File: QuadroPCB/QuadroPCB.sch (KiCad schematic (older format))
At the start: 3 parts

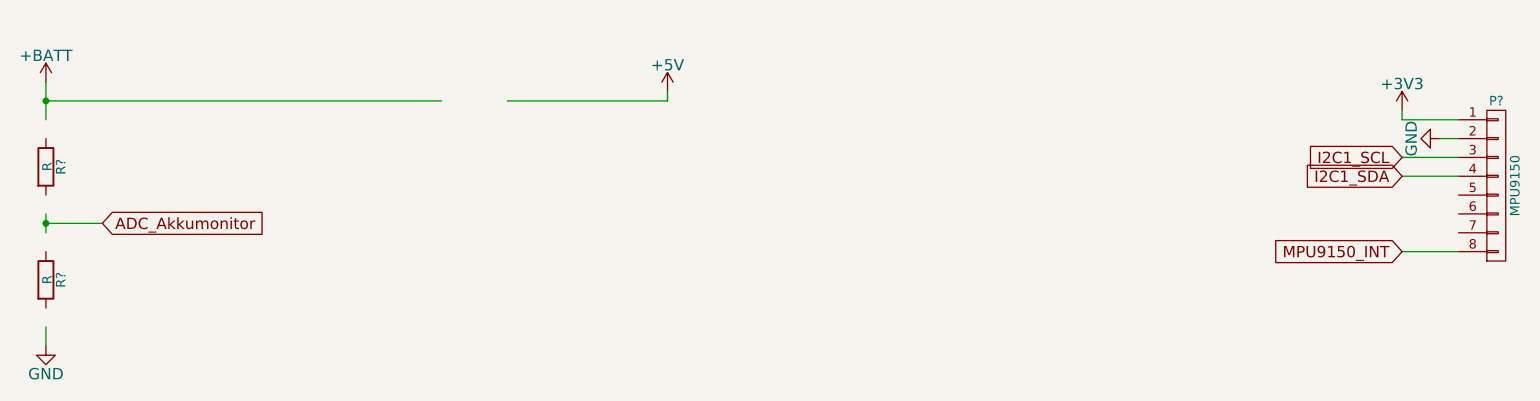
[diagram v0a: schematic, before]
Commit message: added datasheets add step-down converter
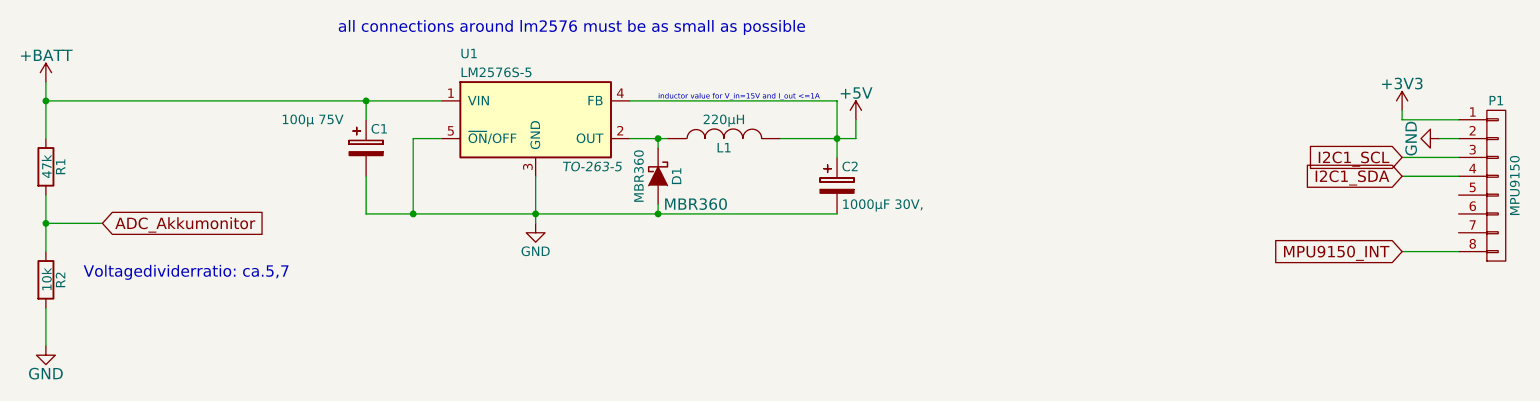
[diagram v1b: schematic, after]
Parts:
- added C1: 100µ 75V, symbol CP
- added C2: 1000µF 30V,, symbol CP
- added D1: MBR360, symbol D_Schottky
- added L1: 220µH, symbol INDUCTOR
- added U1: LM2576S-5, TO-263-5, symbol LM2576S-5
- R1: renamed from R?; value R -> 47k
- R2: renamed from R?; value R -> 10k
- gave numbers to parts that had none: 1
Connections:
- wire segments 13 -> 24
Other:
- note added: "Voltagedividerratio: ca.5,7\n"
- note added: "all connections around lm2576 must be as small as possible"
- note added: "inductor value for V_in=15V and I_out <=1A"
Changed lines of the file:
@@
 LIBS:contrib
 LIBS:valves
+LIBS:dc-dc
+LIBS:stm32
+LIBS:sensors
+LIBS:QuadroPCB-cache
 EELAYER 25 0
 EELAYER END
@@
 $EndDescr
 $Comp
-L R R?
+L R R1
 U 1 1 553FEDF5
 P 1350 1350
-F 0 "R?" V 1430 1350 50  0000 C CNN
-F 1 "R" V 1357 1351 50  0000 C CNN
+F 0 "R1" V 1430 1350 50  0000 C CNN
+F 1 "47k" V 1357 1351 50  0000 C CNN
 F 2 "" V 1280 1350 30  0000 C CNN
 F 3 "" H 1350 1350 30  0000 C CNN
@@
 $EndComp
 $Comp
-L R R?
+L R R2
 U 1 1 553FEF71
 P 1350 1950
-F 0 "R?" V 1430 1950 50  0000 C CNN
-F 1 "R" V 1357 1951 50  0000 C CNN
+F 0 "R2" V 1430 1950 50  0000 C CNN
+F 1 "10k" V 1357 1951 50  0000 C CNN
 F 2 "" V 1280 1950 30  0000 C CNN
 F 3 "" H 1350 1950 30  0000 C CNN
@@
 $EndComp
 $Comp
-L GND #PWR?
+L GND #PWR2
 U 1 1 553FEFAB
 P 1350 2300
-F 0 "#PWR?" H 1350 2050 60  0001 C CNN
+F 0 "#PWR2" H 1350 2050 60  0001 C CNN
 F 1 "GND" H 1350 2150 60  0000 C CNN
 F 2 "" H 1350 2300 60  0000 C CNN
@@
 $EndComp
 $Comp
-L +BATT #PWR?
+L +BATT #PWR1
 U 1 1 553FEFC1
 P 1350 900
-F 0 "#PWR?" H 1350 750 60  0001 C CNN
+F 0 "#PWR1" H 1350 750 60  0001 C CNN
 F 1 "+BATT" H 1350 1040 60  0000 C CNN
 F 2 "" H 1350 900 60  0000 C CNN
@@
 $EndComp
 Wire Wire Line
-	1350 2300 1350 2200
-Wire Wire Line
-	1350 1600 1350 1700
-Wire Wire Line
-	1350 900  1350 1100
+	1350 2100 1350 2300
+Wire Wire Line
+	1350 1500 1350 1800
+Wire Wire Line
+	1350 900  1350 1200
 Text GLabel 1650 1650 2    60   Input ~ 0
 ADC_Akkumonitor
@@
 	1350 1000 3450 1000
 Connection ~ 1350 1000
-Wire Wire Line
-	3800 1000 4650 1000
-$Comp
-L +5V #PWR?
+$Comp
+L +5V #PWR4
 U 1 1 553FF02F
-P 4650 950
-F 0 "#PWR?" H 4650 800 60  0001 C CNN
-F 1 "+5V" H 4650 1090 60  0000 C CNN
-F 2 "" H 4650 950 60  0000 C CNN
-F 3 "" H 4650 950 60  0000 C CNN
-	1    4650 950
-	1    0    0    -1
-$EndComp
-Wire Wire Line
-	4650 1000 4650 950
-$Comp
-L CONN_01X08 P?
+P 5650 1100
+F 0 "#PWR4" H 5650 950 60  0001 C CNN
+F 1 "+5V" H 5650 1240 60  0000 C CNN
+F 2 "" H 5650 1100 60  0000 C CNN
+F 3 "" H 5650 1100 60  0000 C CNN
+	1    5650 1100
+	1    0    0    -1
+$EndComp
+Wire Wire Line
+	5650 1200 5650 1100
+$Comp
+L CONN_01X08 P1
 U 1 1 553FF0BA
 P 9050 1450
-F 0 "P?" H 9050 1900 50  0000 C CNN
+F 0 "P1" H 9050 1900 50  0000 C CNN
 F 1 "MPU9150" V 9150 1450 50  0000 C CNN
 F 2 "" H 9050 1450 60  0000 C CNN
@@
 $EndComp
 $Comp
-L GND #PWR?
+L GND #PWR6
 U 1 1 553FF2AD
 P 8750 1200
-F 0 "#PWR?" H 8750 950 60  0001 C CNN
+F 0 "#PWR6" H 8750 950 60  0001 C CNN
 F 1 "GND" H 8750 1050 60  0000 C CNN
 F 2 "" H 8750 1200 60  0000 C CNN
@@
 $EndComp
 $Comp
-L +3V3 #PWR?
+L +3V3 #PWR5
 U 1 1 553FF331
 P 8550 1050
-F 0 "#PWR?" H 8550 900 60  0001 C CNN
+F 0 "#PWR5" H 8550 900 60  0001 C CNN
 F 1 "+3V3" H 8550 1190 60  0000 C CNN
 F 2 "" H 8550 1050 60  0000 C CNN
@@
 Wire Wire Line
 	8850 1800 8550 1800
+Text Notes 1550 1950 0    60   ~ 0
+Voltagedividerratio: ca.5,7\n
+$Comp
+L LM2576S-5 U1
+U 1 1 5541EC13
+P 3950 1100
+F 0 "U1" H 3550 1450 50  0000 L CNN
+F 1 "LM2576S-5" H 3550 1350 50  0000 L CNN
+F 2 "TO-263-5" H 4250 850 50  0000 C CIN
+F 3 "" H 3950 1100 50  0000 C CNN
+	1    3950 1100
+	1    0    0    -1
+$EndComp
+$Comp
+L GND #PWR3
+U 1 1 5541ECA6
+P 3950 1650
+F 0 "#PWR3" H 3950 1400 50  0001 C CNN
+F 1 "GND" H 3950 1500 50  0000 C CNN
+F 2 "" H 3950 1650 60  0000 C CNN
+F 3 "" H 3950 1650 60  0000 C CNN
+	1    3950 1650
+	1    0    0    -1
+$EndComp
+Wire Wire Line
+	3950 1400 3950 1650
+Wire Wire Line
+	3450 1200 3300 1200
+Wire Wire Line
+	3300 1200 3300 1600
+Wire Wire Line
+	3050 1600 5550 1600
+Connection ~ 3950 1600
+$Comp
+L INDUCTOR L1
+U 1 1 5541EE99
+P 4950 1200
+F 0 "L1" V 4900 1200 50  0000 C CNN
+F 1 "220µH" V 5050 1200 50  0000 C CNN
+F 2 "" H 4950 1200 60  0000 C CNN
+F 3 "" H 4950 1200 60  0000 C CNN
+	1    4950 1200
+	0    -1   -1   0
+$EndComp
+$Comp
+L CP C2
+U 1 1 5541EF3E
+P 5550 1450
+F 0 "C2" H 5575 1550 50  0000 L CNN
+F 1 "1000µF 30V," H 5575 1350 50  0000 L CNN
+F 2 "" H 5588 1300 30  0000 C CNN
+F 3 "" H 5550 1450 60  0000 C CNN
+	1    5550 1450
+	1    0    0    -1
+$EndComp
+$Comp
+L CP C1
+U 1 1 5541EF75
+P 3050 1250
+F 0 "C1" H 3075 1350 50  0000 L CNN
+F 1 "100µ 75V" H 2600 1400 50  0000 L CNN
+F 2 "" H 3088 1100 30  0000 C CNN
+F 3 "" H 3050 1250 60  0000 C CNN
+	1    3050 1250
+	1    0    0    -1
+$EndComp
+Wire Wire Line
+	3050 1400 3050 1600
+Connection ~ 3300 1600
+Wire Wire Line
+	3050 1100 3050 1000
+Connection ~ 3050 1000
+Wire Wire Line
+	4450 1200 4650 1200
+Wire Wire Line
+	5250 1200 5650 1200
+Connection ~ 5550 1200
+$Comp
+L D_Schottky D1
+U 1 1 5541F140
+P 4600 1400
+F 0 "D1" H 4600 1500 50  0000 C CNN
+F 1 "MBR360" H 4600 1300 50  0000 C CNN
+F 2 "" H 4600 1400 60  0000 C CNN
+F 3 "" H 4600 1400 60  0000 C CNN
+F 4 "MBR360" V 4750 1600 60  0000 C CNN "type"
+	1    4600 1400
+	0    1    1    0
+$EndComp
+Wire Wire Line
+	4600 1250 4600 1200
+Connection ~ 4600 1200
+Wire Wire Line
+	4600 1550 4600 1600
+Connection ~ 4600 1600
+Wire Wire Line
+	5550 1000 5550 1300
+Text Notes 2900 650  0    60   ~ 0
+all connections around lm2576 must be as small as possible
+Text Notes 4600 1000 0    28   ~ 0
+inductor value for V_in=15V and I_out <=1A
+Wire Wire Line
+	5550 1000 4450 1000
 $EndSCHEMATC

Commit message: Updated schematic rc receiver, bmp180, motor, eeprom added more datasheets
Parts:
- added IC?: AT24CS02-SSHM, SO8, symbol AT24CS02-SSHM
- added P?: CONN_01X04, symbol CONN_01X04
- added P? (x2): CONN_02X25, symbol CONN_02X25
- added P? (x5): CONN_01X03, symbol CONN_01X03
- added Q?: BSS123, symbol Q_NMOS_DGS
- added R?: 1k, symbol R
- added R? (x2): 10k, symbol R
- added SP?: SPEAKER, symbol SPEAKER
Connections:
- net labels added: +3.3V, Beeper_PIN, I2C2_SCL, I2C2_SDA, MOTOR1, MOTOR2, MOTOR3, MOTOR4, RC_Signal
- wire segments 24 -> 100
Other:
- note added: "BMP180"
- note added: "Beeper"
- note added: "EEPROM\n"
- note added: "MPU9150"
- note added: "Motor Connectors\n"
- note added: "Power\n"
- note added: "RC Receiver"
- note added: "STM32F3 Discovery\n\nPin Headers\n"
- note added: "left\n"
- note added: "right\n"
- moved on the sheet: C1, C2, D1, L1, P1, R1, R2, U1

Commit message: updated connections
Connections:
- net labels added: PA1, PA10, PA9, PB6, PB7, PB8, PC6, PC7, PC8, PC9, PE4
- wire segments 100 -> 123
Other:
- note added: "Connections\n"
- note added: "TODO:\n\nbuzzer pin\nweite pins rausführen?\n"
- moved on the sheet: P?

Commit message: blub
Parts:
- removed Q?: BSS123, symbol Q_NMOS_DGS
- added P10: AKKU, Wire_Connections_Bridges:WireConnection_1-2mmDrill, symbol CONN_01X02
- added Q1: Q_NMOS_GSD, Housings_SOT-23_SOT-143_TSOT-6:SOT-23_Handsoldering, symbol Q_NMOS_GSD
- C1: value 100µ 75V -> 100µ 25V; footprint (none) -> Capacitors_SMD:c_elec_6.3x7.7
- C2: value 1000µF 30V, -> 680µF 10V; footprint (none) -> Capacitors_SMD:c_elec_8x10
- D1: footprint (none) -> Diodes_SMD:Diode-DO-214BA
- IC1: renamed from IC?; footprint SO8 -> Sockets_DIP:DIP-8__300_ELL
- L1: footprint (none) -> Choke_SMD:Choke_SMD_PISR_Handsoldering_FASTRON
- P1: footprint (none) -> Pin_Headers:Pin_Header_Straight_1x08
- P2: renamed from P?; value CONN_02X25 -> stm32discovery_left; footprint (none) -> Pin_Headers:Pin_Header_Straight_2x25
- P3: renamed from P?; value CONN_02X25 -> stm32discovery_right; footprint (none) -> Pin_Headers:Pin_Header_Straight_2x25
- P4: renamed from P?; value CONN_01X03 -> rc_signal; footprint (none) -> Pin_Headers:Pin_Header_Straight_1x03
- P5: renamed from P?; value CONN_01X03 -> Motor3; footprint (none) -> Pin_Headers:Pin_Header_Straight_1x03
- P6: renamed from P?; value CONN_01X03 -> Motor4; footprint (none) -> Pin_Headers:Pin_Header_Straight_1x03
- P7: renamed from P?; value CONN_01X04 -> BMP180; footprint (none) -> Pin_Headers:Pin_Header_Straight_1x04
- P8: renamed from P?; value CONN_01X03 -> Motor1; footprint (none) -> Pin_Headers:Pin_Header_Straight_1x03
- P9: renamed from P?; value CONN_01X03 -> Motor2; footprint (none) -> Pin_Headers:Pin_Header_Straight_1x03
- R1, R2: footprint (none) -> Resistors_SMD:R_0805_HandSoldering
- R3, R4, R5: renamed from R?; footprint (none) -> Resistors_SMD:R_0805_HandSoldering
- SP1: renamed from SP?; footprint (none) -> Buzzers_Beepers:Buzzer_12x9.5RM7.6
- U1: footprint TO-263-5 -> SMD_Packages:TO-263-5_HandSoldering
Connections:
- net labels added: power_gnd, pwr
- wire segments 123 -> 109
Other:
- moved on the sheet: R1, R2

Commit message: dei mudder commitet
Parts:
- P10: footprint Wire_Connections_Bridges:WireConnection_1-2mmDrill -> Connect:PINHEAD1-2
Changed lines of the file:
@@
 F 0 "P10" H 1000 1750 50  0000 C CNN
 F 1 "AKKU" V 1100 1600 50  0000 C CNN
-F 2 "Wire_Connections_Bridges:WireConnection_1-2mmDrill" H 1000 1600 60  0001 C CNN
+F 2 "Connect:PINHEAD1-2" H 1000 1600 60  0001 C CNN
 F 3 "" H 1000 1600 60  0000 C CNN
 	1    1000 1600

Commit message: neuer step down
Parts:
- removed U1: LM2576S-5, SMD_Packages:TO-263-5_HandSoldering, symbol LM2576S-5
- added C3: 10nF, Capacitors_SMD:C_0805_HandSoldering, symbol C
- added U1: LM2675M-5, SMD_Packages:SOIC-8-N, symbol LM2675M-5
- C1: value 100µ 25V -> 220µF 25V; footprint Capacitors_SMD:c_elec_6.3x7.7 -> Capacitors_SMD:c_elec_8x10.5
- C2: value 680µF 10V -> 100µF 10V; footprint Capacitors_SMD:c_elec_8x10 -> Capacitors_SMD:c_elec_8x6.7
- D1: value MBR360 -> MBRS340; footprint Diodes_SMD:Diode-DO-214BA -> Diodes_SMD:Diode-DO-214AB_Handsoldering; type MBR360 -> (none)
- L1: value 220µH -> 33µH 1,4 A; footprint Choke_SMD:Choke_SMD_PISR_Handsoldering_FASTRON -> Choke_SMD:Choke_SMD_PISN_Handsoldering_FASTRON
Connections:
- net +5V: now also U1.4 (FB)
- net +BATT: now also U1.7 (VIN)
- net GND: now also U1.6 (GND)
- net pwr: no longer names the net of D1.1 (K), L1.1
- net pwr: now also C3.1, U1.8 (VSW)
- new net: C3.2, U1.1 (CB)
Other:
- note removed: "all connections around lm2576 must be as small as possible"
- note removed: "inductor value for V_in=15V and I_out <=1A"
- moved on the sheet: D1, L1
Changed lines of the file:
@@
 $EndComp
 $Comp
-L GND #PWR01
+L GND #PWR5
 U 1 1 553FEFAB
 P 1550 2150
-F 0 "#PWR01" H 1550 1900 60  0001 C CNN
+F 0 "#PWR5" H 1550 1900 60  0001 C CNN
 F 1 "GND" H 1550 2000 60  0000 C CNN
 F 2 "" H 1550 2150 60  0000 C CNN
@@
 $EndComp
 $Comp
-L +BATT #PWR02
+L +BATT #PWR4
 U 1 1 553FEFC1
 P 1550 1000
-F 0 "#PWR02" H 1550 850 60  0001 C CNN
+F 0 "#PWR4" H 1550 850 60  0001 C CNN
 F 1 "+BATT" H 1550 1140 60  0000 C CNN
 F 2 "" H 1550 1000 60  0000 C CNN
@@
 	1900 1600 1550 1600
 Connection ~ 1550 1600
-Wire Wire Line
-	1350 1100 3200 1100
 Connection ~ 1550 1100
 $Comp
-L +5V #PWR03
+L +5V #PWR11
 U 1 1 553FF02F
 P 5400 1200
-F 0 "#PWR03" H 5400 1050 60  0001 C CNN
+F 0 "#PWR11" H 5400 1050 60  0001 C CNN
 F 1 "+5V" H 5400 1340 60  0000 C CNN
 F 2 "" H 5400 1200 60  0000 C CNN
@@
 $EndComp
 $Comp
-L GND #PWR04
+L GND #PWR15
 U 1 1 553FF2AD
 P 8700 1150
-F 0 "#PWR04" H 8700 900 60  0001 C CNN
+F 0 "#PWR15" H 8700 900 60  0001 C CNN
 F 1 "GND" H 8700 1000 60  0000 C CNN
 F 2 "" H 8700 1150 60  0000 C CNN
@@
 $EndComp
 $Comp
-L +3V3 #PWR05
+L +3V3 #PWR14
 U 1 1 553FF331
 P 8500 1000
-F 0 "#PWR05" H 8500 850 60  0001 C CNN
+F 0 "#PWR14" H 8500 850 60  0001 C CNN
 F 1 "+3V3" H 8500 1140 60  0000 C CNN
 F 2 "" H 8500 1000 60  0000 C CNN
@@
 Voltagedividerratio: ca.5,7\n
 $Comp
-L LM2576S-5 U1
-U 1 1 5541EC13
-P 3700 1200
-F 0 "U1" H 3300 1550 50  0000 L CNN
-F 1 "LM2576S-5" H 3300 1450 50  0000 L CNN
-F 2 "SMD_Packages:TO-263-5_HandSoldering" H 4000 950 50  0000 C CIN
-F 3 "" H 3700 1200 50  0000 C CNN
-	1    3700 1200
-	1    0    0    -1
-$EndComp
-$Comp
-L GND #PWR06
+L GND #PWR10
 U 1 1 5541ECA6
 P 3700 1750
-F 0 "#PWR06" H 3700 1500 50  0001 C CNN
+F 0 "#PWR10" H 3700 1500 50  0001 C CNN
 F 1 "GND" H 3700 1600 50  0000 C CNN
 F 2 "" H 3700 1750 60  0000 C CNN
@@
 $EndComp
 Wire Wire Line
-	3700 1500 3700 1750
-Wire Wire Line
-	3200 1300 3050 1300
-Wire Wire Line
-	3050 1300 3050 1700
-Wire Wire Line
 	2800 1700 5300 1700
 Connection ~ 3700 1700
@@
 L INDUCTOR L1
 U 1 1 5541EE99
-P 4700 1300
-F 0 "L1" V 4650 1300 50  0000 C CNN
-F 1 "220µH" V 4800 1300 50  0000 C CNN
-F 2 "Choke_SMD:Choke_SMD_PISR_Handsoldering_FASTRON" H 4700 1300 60  0001 C CNN
-F 3 "" H 4700 1300 60  0000 C CNN
-	1    4700 1300
+P 4900 1300
+F 0 "L1" V 4850 1300 50  0000 C CNN
+F 1 "33µH 1,4 A" V 5000 1300 50  0000 C CNN
+F 2 "Choke_SMD:Choke_SMD_PISN_Handsoldering_FASTRON" H 4900 1300 60  0001 C CNN
+F 3 "" H 4900 1300 60  0000 C CNN
+	1    4900 1300
 	0    -1   -1   0
 $EndComp
@@
 P 5300 1550
 F 0 "C2" H 5325 1650 50  0000 L CNN
-F 1 "680µF 10V" H 5325 1450 50  0000 L CNN
-F 2 "Capacitors_SMD:c_elec_8x10" H 5338 1400 30  0001 C CNN
+F 1 "100µF 10V" H 5325 1450 50  0000 L CNN
+F 2 "Capacitors_SMD:c_elec_8x6.7" H 5338 1400 30  0001 C CNN
 F 3 "" H 5300 1550 60  0000 C CNN
 	1    5300 1550
@@
 P 2800 1350
 F 0 "C1" H 2825 1450 50  0000 L CNN
-F 1 "100µ 25V" H 2350 1500 50  0000 L CNN
-F 2 "Capacitors_SMD:c_elec_6.3x7.7" H 2838 1200 30  0001 C CNN
+F 1 "220µF 25V" H 2350 1500 50  0000 L CNN
+F 2 "Capacitors_SMD:c_elec_8x10.5" H 2838 1200 30  0001 C CNN
 F 3 "" H 2800 1350 60  0000 C CNN
 	1    2800 1350
@@
 Wire Wire Line
 	2800 1500 2800 1700
-Connection ~ 3050 1700
-Wire Wire Line
-	2800 1200 2800 1100
+Wire Wire Line
+	2800 900  2800 1200
 Connection ~ 2800 1100
 Wire Wire Line
-	4200 1300 4400 1300
-Wire Wire Line
-	5000 1300 5400 1300
+	4200 1300 4600 1300
+Wire Wire Line
+	5200 1300 5400 1300
 Connection ~ 5300 1300
 $Comp
 L D_Schottky D1
 U 1 1 5541F140
-P 4350 1500
-F 0 "D1" H 4350 1600 50  0000 C CNN
-F 1 "MBR360" H 4350 1400 50  0000 C CNN
-F 2 "Diodes_SMD:Diode-DO-214BA" H 4350 1500 60  0001 C CNN
-F 3 "" H 4350 1500 60  0000 C CNN
-F 4 "MBR360" V 4500 1700 60  0000 C CNN "type"
-	1    4350 1500
+P 4550 1500
+F 0 "D1" H 4550 1600 50  0000 C CNN
+F 1 "MBRS340" H 4550 1400 50  0000 C CNN
+F 2 "Diodes_SMD:Diode-DO-214AB_Handsoldering" H 4550 1500 60  0001 C CNN
+F 3 "" H 4550 1500 60  0000 C CNN
+	1    4550 1500
 	0    1    1    0
 $EndComp
 Wire Wire Line
-	4350 1350 4350 1300
-Connection ~ 4350 1300
-Wire Wire Line
-	4350 1650 4350 1700
-Connection ~ 4350 1700
-Wire Wire Line
-	5300 1100 5300 1400
-Text Notes 2650 750  0    60   ~ 0
-all connections around lm2576 must be as small as possible
-Text Notes 4350 1100 0    28   ~ 0
-inductor value for V_in=15V and I_out <=1A
-Wire Wire Line
-	5300 1100 4200 1100
+	4550 1100 4550 1350
+Connection ~ 4550 1300
+Wire Wire Line
+	4550 1650 4550 1700
+Connection ~ 4550 1700
 $Comp
 L R R4
@@
 $EndComp
 $Comp
-L +5V #PWR07
+L +5V #PWR22
 U 1 1 554200B8
 P 10600 900
-F 0 "#PWR07" H 10600 750 50  0001 C CNN
+F 0 "#PWR22" H 10600 750 50  0001 C CNN
 F 1 "+5V" H 10600 1040 50  0000 C CNN
 F 2 "" H 10600 900 60  0000 C CNN
@@
 $EndComp
 $Comp
-L GND #PWR08
+L GND #PWR23
 U 1 1 55420164
 P 10600 1750
-F 0 "#PWR08" H 10600 1500 50  0001 C CNN
+F 0 "#PWR23" H 10600 1500 50  0001 C CNN
 F 1 "GND" H 10600 1600 50  0000 C CNN
 F 2 "" H 10600 1750 60  0000 C CNN
@@
 $EndComp
 $Comp
-L GND #PWR09
+L GND #PWR21
 U 1 1 55420E59
 P 10400 2600
-F 0 "#PWR09" H 10400 2350 60  0001 C CNN
+F 0 "#PWR21" H 10400 2350 60  0001 C CNN
 F 1 "GND" H 10400 2450 60  0000 C CNN
 F 2 "" H 10400 2600 60  0000 C CNN
@@
 $EndComp
 $Comp
-L +3V3 #PWR010
+L +3V3 #PWR18
 U 1 1 5542137E
 P 10000 3350
-F 0 "#PWR010" H 10000 3200 60  0001 C CNN
+F 0 "#PWR18" H 10000 3200 60  0001 C CNN
 F 1 "+3V3" H 10000 3490 60  0000 C CNN
 F 2 "" H 10000 3350 60  0000 C CNN
@@
 $EndComp
 $Comp
-L GND #PWR011
+L GND #PWR19
 U 1 1 554213A3
 P 10000 4200
-F 0 "#PWR011" H 10000 3950 60  0001 C CNN
+F 0 "#PWR19" H 10000 3950 60  0001 C CNN
 F 1 "GND" H 10000 4050 60  0000 C CNN
 F 2 "" H 10000 4200 60  0000 C CNN
@@
 $EndComp
 $Comp
-L +3V3 #PWR012
+L +3V3 #PWR20
 U 1 1 55420E36
 P 10300 2300
-F 0 "#PWR012" H 10300 2150 60  0001 C CNN
+F 0 "#PWR20" H 10300 2150 60  0001 C CNN
 F 1 "+3V3" H 10300 2440 60  0000 C CNN
 F 2 "" H 10300 2300 60  0000 C CNN
@@
 	3600 2550 700  2550
 $Comp
-L +3V3 #PWR013
+L +3V3 #PWR1
 U 1 1 55422E4A
 P 1100 3300
-F 0 "#PWR013" H 1100 3150 60  0001 C CNN
+F 0 "#PWR1" H 1100 3150 60  0001 C CNN
 F 1 "+3V3" H 1100 3440 60  0000 C CNN
 F 2 "" H 1100 3300 60  0000 C CNN
@@
 $EndComp
 $Comp
-L +3V3 #PWR014
+L +3V3 #PWR6
 U 1 1 55422ECC
 P 1850 3300
-F 0 "#PWR014" H 1850 3150 60  0001 C CNN
+F 0 "#PWR6" H 1850 3150 60  0001 C CNN
 F 1 "+3V3" H 1850 3440 60  0000 C CNN
 F 2 "" H 1850 3300 60  0000 C CNN
@@
 $EndComp
 $Comp
-L GND #PWR015
+L GND #PWR2
 U 1 1 5542303C
 P 1100 3500
-F 0 "#PWR015" H 1100 3250 50  0001 C CNN
+F 0 "#PWR2" H 1100 3250 50  0001 C CNN
 F 1 "GND" H 1100 3350 50  0000 C CNN
 F 2 "" H 1100 3500 60  0000 C CNN
@@
 $EndComp
 $Comp
-L GND #PWR016
+L GND #PWR3
 U 1 1 55423070
 P 1150 6000
-F 0 "#PWR016" H 1150 5750 50  0001 C CNN
+F 0 "#PWR3" H 1150 5750 50  0001 C CNN
 F 1 "GND" H 1150 5850 50  0000 C CNN
 F 2 "" H 1150 6000 60  0000 C CNN
@@
 	1850 3400 1850 3300
 $Comp
-L +5V #PWR017
+L +5V #PWR7
 U 1 1 554236B8
 P 2400 3300
-F 0 "#PWR017" H 2400 3150 60  0001 C CNN
+F 0 "#PWR7" H 2400 3150 60  0001 C CNN
 F 1 "+5V" H 2400 3440 60  0000 C CNN
 F 2 "" H 2400 3300 60  0000 C CNN
@@
 	2400 3400 2400 3300
 $Comp
-L +5V #PWR018
+L +5V #PWR9
 U 1 1 554237F2
 P 3100 3300
-F 0 "#PWR018" H 3100 3150 60  0001 C CNN
+F 0 "#PWR9" H 3100 3150 60  0001 C CNN
 F 1 "+5V" H 3100 3440 60  0000 C CNN
 F 2 "" H 3100 3300 60  0000 C CNN
@@
 	3100 3400 3100 3300
 $Comp
-L GND #PWR019
+L GND #PWR8
 U 1 1 554239AA
 P 2450 6000
-F 0 "#PWR019" H 2450 5750 50  0001 C CNN
+F 0 "#PWR8" H 2450 5750 50  0001 C CNN
 F 1 "GND" H 2450 5850 50  0000 C CNN
 F 2 "" H 2450 6000 60  0000 C CNN
@@
 $EndComp
 $Comp
-L +3.3V #PWR020
+L +3.3V #PWR12
 U 1 1 55423C5D
 P 6500 950
-F 0 "#PWR020" H 6500 800 50  0001 C CNN
+F 0 "#PWR12" H 6500 800 50  0001 C CNN
 F 1 "+3.3V" H 6500 1090 50  0000 C CNN
 F 2 "" H 6500 950 60  0000 C CNN
@@
 $EndComp
 $Comp
-L GND #PWR021
+L GND #PWR13
 U 1 1 55423C83
 P 7100 1100
-F 0 "#PWR021" H 7100 850 50  0001 C CNN
+F 0 "#PWR13" H 7100 850 50  0001 C CNN
 F 1 "GND" H 7100 950 50  0000 C CNN
 F 2 "" H 7100 1100 60  0000 C CNN
@@
 MOTOR4
 $Comp
-L GND #PWR022
+L GND #PWR17
 U 1 1 554248D9
 P 9700 5550
-F 0 "#PWR022" H 9700 5300 50  0001 C CNN
+F 0 "#PWR17" H 9700 5300 50  0001 C CNN
 F 1 "GND" H 9700 5400 50  0000 C CNN
 F 2 "" H 9700 5550 60  0000 C CNN
@@
 $EndComp
 $Comp
-L GND #PWR023
+L GND #PWR16
 U 1 1 55424917
 P 9700 5050
-F 0 "#PWR023" H 9700 4800 50  0001 C CNN
+F 0 "#PWR16" H 9700 4800 50  0001 C CNN
 F 1 "GND" H 9700 4900 50  0000 C CNN
 F 2 "" H 9700 5050 60  0000 C CNN
@@
 $EndComp
 $Comp
-L GND #PWR024
+L GND #PWR25
 U 1 1 5542494E
 P 10600 5600
-F 0 "#PWR024" H 10600 5350 50  0001 C CNN
+F 0 "#PWR25" H 10600 5350 50  0001 C CNN
 F 1 "GND" H 10600 5450 50  0000 C CNN
 F 2 "" H 10600 5600 60  0000 C CNN
@@
 $EndComp
 $Comp
-L GND #PWR025
+L GND #PWR24
 U 1 1 5542499B
 P 10600 5050
-F 0 "#PWR025" H 10600 4800 50  0001 C CNN
+F 0 "#PWR24" H 10600 4800 50  0001 C CNN
 F 1 "GND" H 10600 4900 50  0000 C CNN
 F 2 "" H 10600 5050 60  0000 C CNN
@@
 Wire Wire Line
 	1350 1550 1350 1100
-Text Label 3300 1700 0    60   ~ 0
-power_gnd
-Text Label 4250 1300 0    60   ~ 0
-pwr
+$Comp
+L LM2675M-5 U1
+U 1 1 55461C96
+P 3700 1100
+F 0 "U1" H 3300 1550 50  0000 L CNN
+F 1 "LM2675M-5" H 3300 1450 50  0000 L CNN
+F 2 "SMD_Packages:SOIC-8-N" H 4000 750 50  0000 C CIN
+F 3 "" H 3700 1100 50  0000 C CNN
+	1    3700 1100
+	1    0    0    -1
+$EndComp
+Wire Wire Line
+	3700 1500 3700 1750
+Wire Wire Line
+	3200 900  2800 900
+Wire Wire Line
+	1350 1100 2800 1100
+$Comp
+L C C3
+U 1 1 554623AC
+P 4400 1100
+F 0 "C3" H 4425 1200 50  0000 L CNN
+F 1 "10nF" H 4425 1000 50  0000 L CNN
+F 2 "Capacitors_SMD:C_0805_HandSoldering" H 4438 950 30  0001 C CNN
+F 3 "" H 4400 1100 60  0000 C CNN
+	1    4400 1100
+	0    1    1    0
+$EndComp
+Wire Wire Line
+	4200 1100 4250 1100
+Wire Wire Line
+	4200 900  5300 900
+Wire Wire Line
+	5300 900  5300 1400
 $EndSCHEMATC
